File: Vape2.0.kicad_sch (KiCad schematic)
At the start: 0 parts

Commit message: finished schematics
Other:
- sheet boost_converter ports: added V_SENSE; removed none
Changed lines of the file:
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@@
+	(wire
+		(pts
+			(xy 236.22 119.38) (xy 236.3866 119.38)
+		)
+		(stroke
+			(width 0)
+			(type default)
+		)
+	)
 	(wire
 		(pts
@@
 	(wire
 		(pts
+			(xy 236.3866 119.38) (xy 236.3866 159.004)
+		)
+		(stroke
+			(width 0)
+			(type default)
+		)
+	)
+	(wire
+		(pts
 			(xy 261.5947 83.82) (xy 250.19 83.82)
 		)
@@
 		(pts
 			(xy 245.3547 156.464) (xy 254 156.464)
+		)
+		(stroke
+			(width 0)
+			(type default)
+		)
+	)
+	(wire
+		(pts
+			(xy 236.3866 159.004) (xy 254 159.004)
 		)
 		(stroke
@@
 			)
 		)
+		(pin "V_SENSE" output
+			(at 236.22 119.38 0)
+			(effects
+				(font
+					(size 1.27 1.27)
+				)
+				(justify right)
+			)
+		)

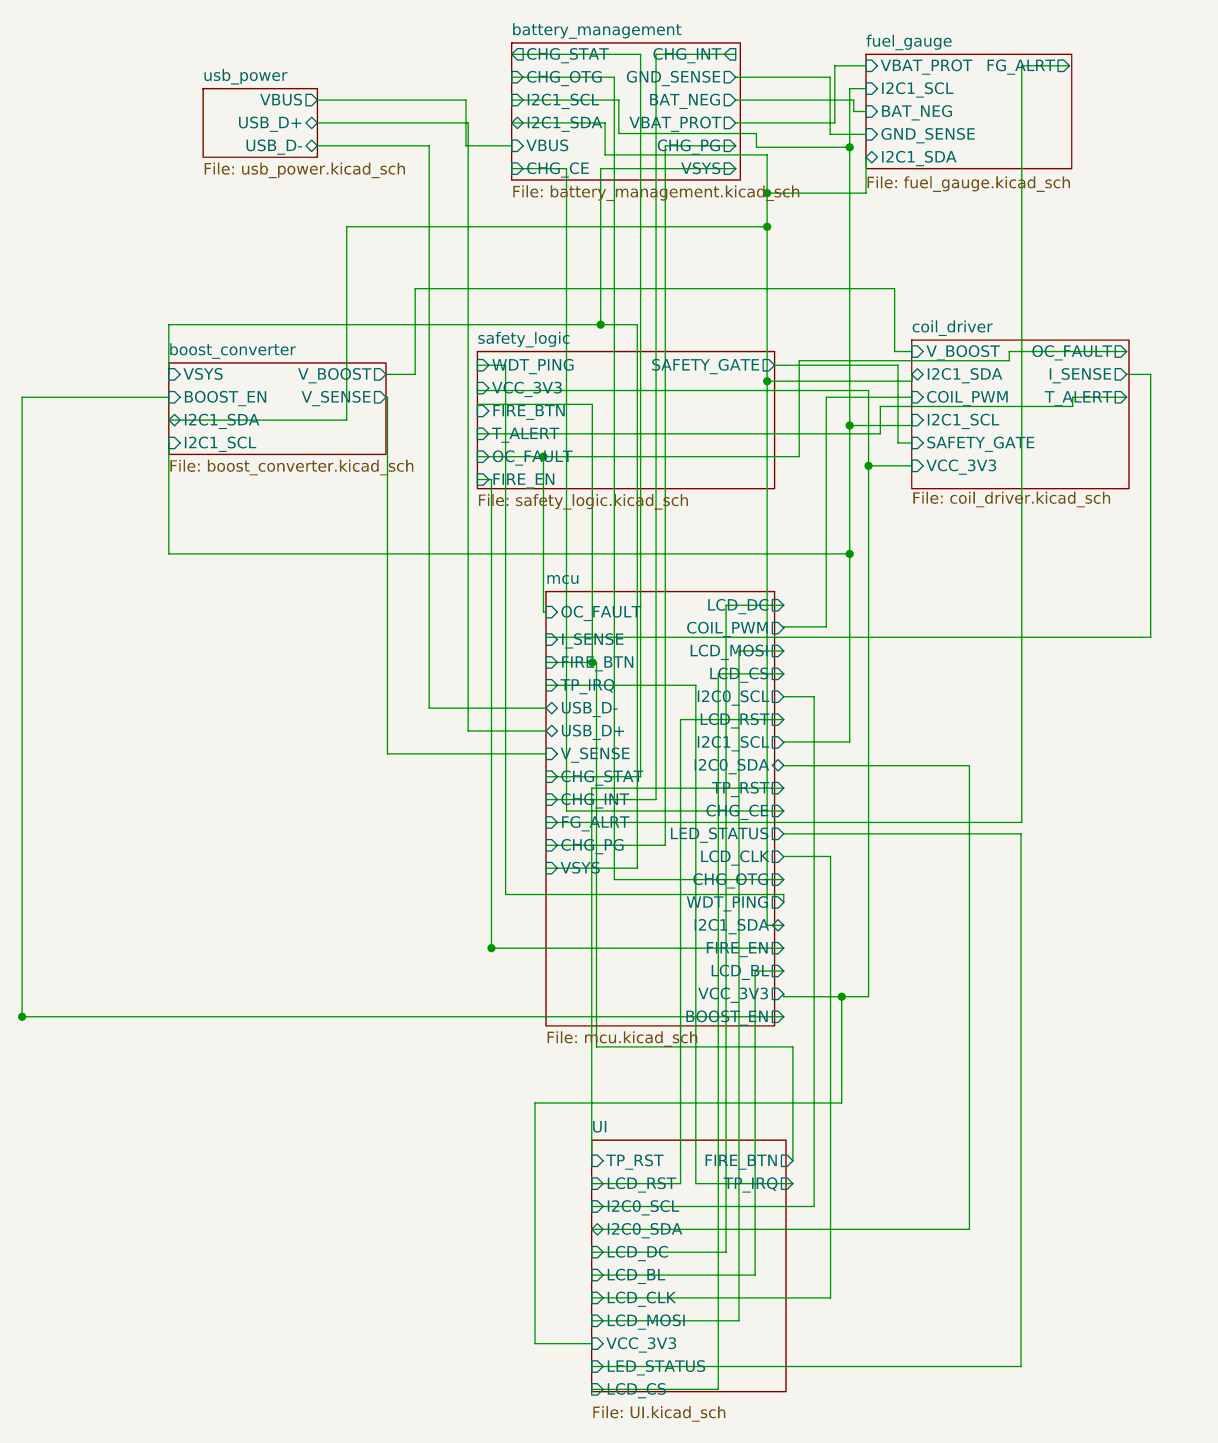
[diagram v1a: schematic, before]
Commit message: fix missing connections, complete footprints
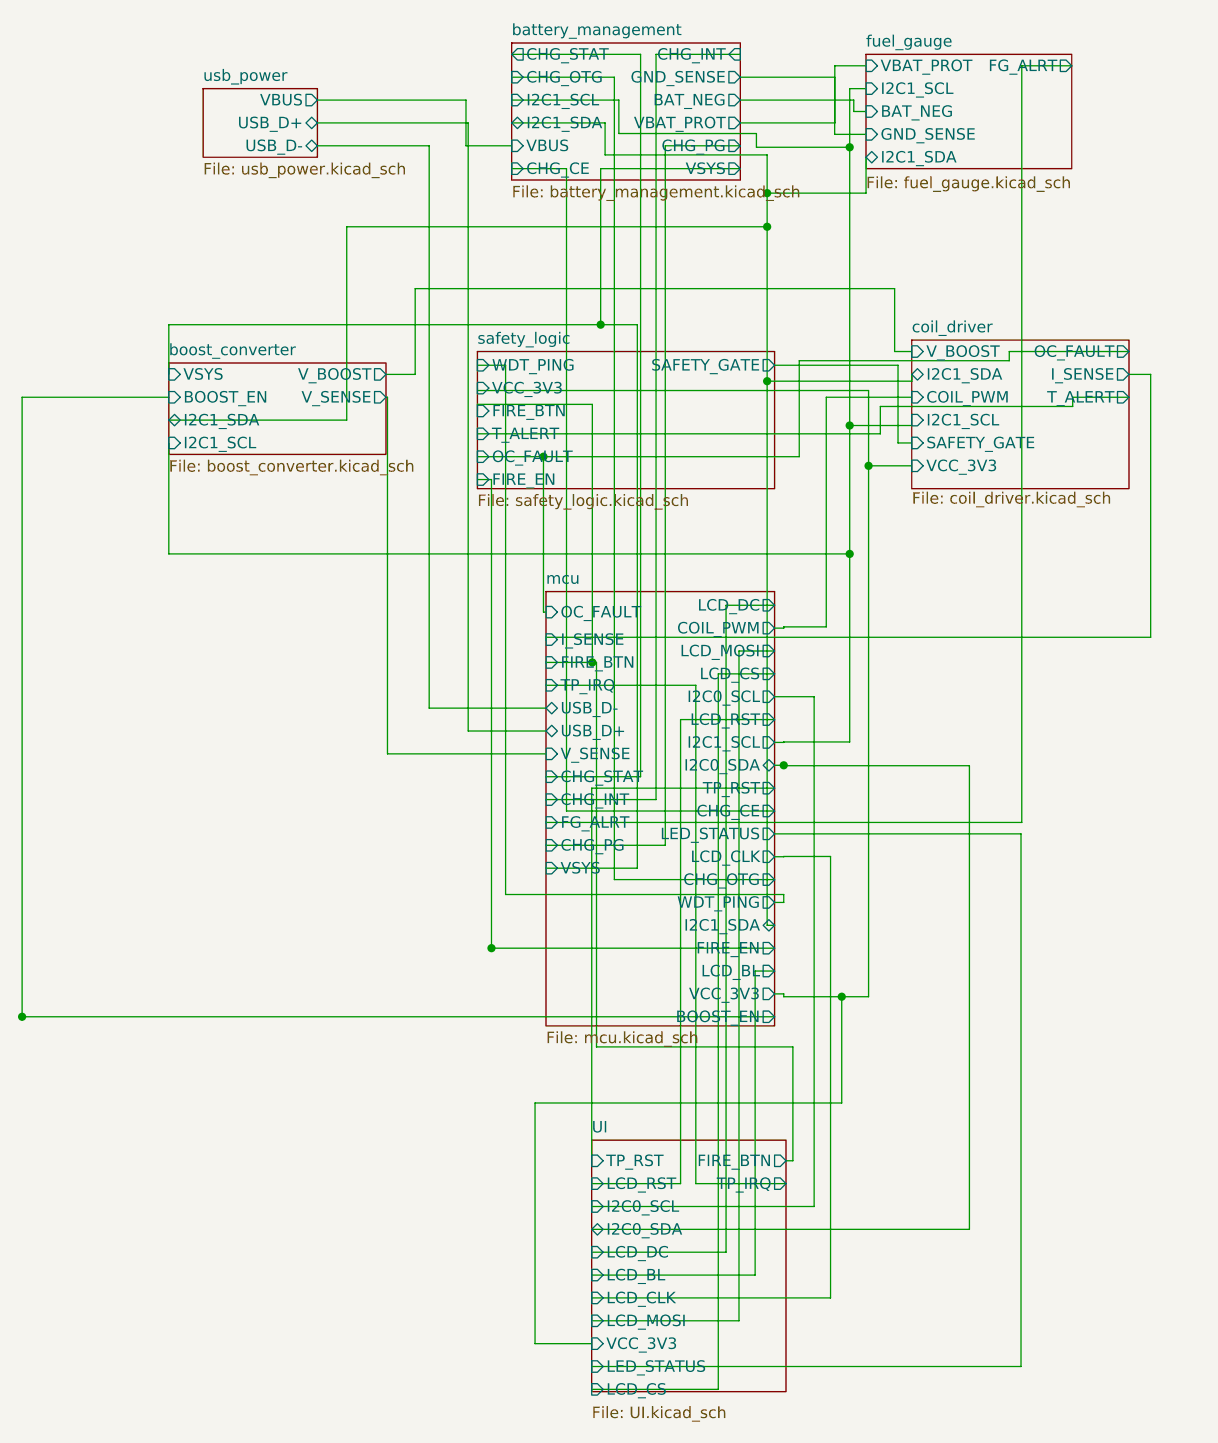
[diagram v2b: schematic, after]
